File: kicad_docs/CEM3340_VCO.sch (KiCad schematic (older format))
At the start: 94 parts, among them J1 tuning controls, J2 1 v/oct inputs, J3 linear FM input, J4 sync input, J5 PWM inputs, J6 power input, Q1 MMDT3904, U1 L78L10_SOT89, U2 MC7905, U3 REF02AU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

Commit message: extract circuit blocks into separate schem pages
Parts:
- removed C1, C16, C17: 100nF, Capacitor_SMD:C_0805_2012Metric_Pad1.15x1.40mm_HandSolder, symbol Device:C
- removed C10, C13, C14: 1nF, Capacitor_SMD:C_0805_2012Metric_Pad1.15x1.40mm_HandSolder, symbol Device:C
- removed C11, C15: 10nF, Capacitor_SMD:C_0805_2012Metric_Pad1.15x1.40mm_HandSolder, symbol Device:C
- removed C20: 560pF, Capacitor_SMD:C_0805_2012Metric_Pad1.15x1.40mm_HandSolder, symbol Device:C
- removed C25: 10pF, Capacitor_SMD:C_0805_2012Metric_Pad1.15x1.40mm_HandSolder, symbol Device:C
- removed J1: tuning controls, Connector_PinHeader_2.54mm:PinHeader_1x05_P2.54mm_Vertical, symbol Connector_Generic:Conn_01x05
- removed J2: 1 v/oct inputs, Connector_PinHeader_2.54mm:PinHeader_1x04_P2.54mm_Vertical, symbol Connector_Generic:Conn_01x04
- removed J3: linear FM input, Connector_PinHeader_2.54mm:PinHeader_1x02_P2.54mm_Vertical, symbol Connector_Generic:Conn_01x02
- removed J4: sync input, Connector_PinHeader_2.54mm:PinHeader_1x02_P2.54mm_Vertical, symbol Connector_Generic:Conn_01x02
- removed J5: PWM inputs, Connector_PinHeader_2.54mm:PinHeader_1x05_P2.54mm_Vertical, symbol Connector_Generic:Conn_01x05
- removed JP1: sync sel 1, Jumper:SolderJumper-3_P1.3mm_Open_RoundedPad1.0x1.5mm, symbol Jumper:SolderJumper_3_Open
- removed JP2: sync sel 2, Jumper:SolderJumper-3_P1.3mm_Open_RoundedPad1.0x1.5mm, symbol Jumper:SolderJumper_3_Open
- removed Q1: MMDT3904, Package_TO_SOT_SMD:SOT-363_SC-70-6_Handsoldering, symbol Transistor_BJT:MMDT3904
- removed R1, R2, R29, R3, R31, R33, R37, R38, R7: 100k, Resistor_SMD:R_0805_2012Metric_Pad1.15x1.40mm_HandSolder, symbol Device:R
- removed R10, R9: 5k6, Resistor_SMD:R_0805_2012Metric_Pad1.15x1.40mm_HandSolder, symbol Device:R
- removed R11, R8: 1M, Resistor_SMD:R_0805_2012Metric_Pad1.15x1.40mm_HandSolder, symbol Device:R
- removed R12, R13: 51k, Resistor_SMD:R_0805_2012Metric_Pad1.15x1.40mm_HandSolder, symbol Device:R
- removed R15, R26: 18k, Resistor_SMD:R_0805_2012Metric_Pad1.15x1.40mm_HandSolder, symbol Device:R
- removed R16: 82k, Resistor_SMD:R_0805_2012Metric_Pad1.15x1.40mm_HandSolder, symbol Device:R
- removed R17, R20: 470, Resistor_SMD:R_0805_2012Metric_Pad1.15x1.40mm_HandSolder, symbol Device:R
- removed R19: 680k, Resistor_SMD:R_0805_2012Metric_Pad1.15x1.40mm_HandSolder, symbol Device:R
- removed R21: 1k62, Resistor_SMD:R_0805_2012Metric_Pad1.15x1.40mm_HandSolder, symbol Device:R
- removed R22: 27k, Resistor_SMD:R_0805_2012Metric_Pad1.15x1.40mm_HandSolder, symbol Device:R
- removed R23, R28: 2k2, Resistor_SMD:R_0805_2012Metric_Pad1.15x1.40mm_HandSolder, symbol Device:R
- removed R24, R27, R34: 10k, Resistor_SMD:R_0805_2012Metric_Pad1.15x1.40mm_HandSolder, symbol Device:R
- removed R25: 390, Resistor_SMD:R_0805_2012Metric_Pad1.15x1.40mm_HandSolder, symbol Device:R
- removed R30, R32, R4, R5: ???, Resistor_SMD:R_0805_2012Metric_Pad1.15x1.40mm_HandSolder, symbol Device:R
- removed R35, R36: 11k, Resistor_SMD:R_0805_2012Metric_Pad1.15x1.40mm_HandSolder, symbol Device:R
- removed R39: 10M, Resistor_SMD:R_0805_2012Metric_Pad1.15x1.40mm_HandSolder, symbol Device:R
- removed R40, R44: R, Resistor_SMD:R_0805_2012Metric_Pad1.15x1.40mm_HandSolder, symbol Device:R
- removed R41, R42, R43: 1k, Resistor_SMD:R_0805_2012Metric_Pad1.15x1.40mm_HandSolder, symbol Device:R
- removed R6: 270k, Resistor_SMD:R_0805_2012Metric_Pad1.15x1.40mm_HandSolder, symbol Device:R
- removed RV1: 20k, Potentiometer_THT:Potentiometer_Bourns_3296W_Vertical, symbol Device:R_POT_TRIM
- removed RV2: 5k, Potentiometer_THT:Potentiometer_Bourns_3296W_Vertical, symbol Device:R_POT_TRIM
- removed RV3, RV5, RV6: 50k, Potentiometer_THT:Potentiometer_Bourns_3296W_Vertical, symbol Device:R_POT_TRIM
- removed RV4: 500, Potentiometer_THT:Potentiometer_Bourns_3296W_Vertical, symbol Device:R_POT_TRIM
- removed TP1, TP2: TestPoint, TestPoint:TestPoint_Keystone_5000-5004_Miniature, symbol Connector:TestPoint
- removed U4: CEM3340, Package_DIP:DIP-16_W7.62mm, symbol my_parts:CEM3340
- removed unit 1 of U5
- removed unit 2 of U5
- removed unit 2 of U6
- removed unit 1 of U6
- removed unit 1 of U7
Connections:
- net buffered_pulse_out renamed Waveshapers/10vpp_pulse_v_out
- net buffered_saw_out renamed Waveshapers/10vpp_saw_v_out
- net buffered_sine_out renamed Waveshapers/10vpp_sine_v_out
- net buffered_tri_out renamed Waveshapers/10vpp_triangle_v_out
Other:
- note removed: "PWM CV"
- note removed: "Power supply"
- note removed: "Signal Inputs"
- note removed: "Signal Outputs"
- note removed: "VCO Core"
- note removed: "Waveshapers/Output Buffers"
- note removed: "about ???vpp"
- note removed: "coarse tune"
- note removed: "fine tune"
- note removed: "freq offset adj"
- note removed: "high freq adj"
- note removed: "manual pulse width"
- note removed: "pulse shaper/buffer"
- note removed: "saw wave amp/buffer"
- note removed: "scale adj"
- note removed: "sine shape adj"
- note removed: "sine symm adj"
- note removed: "tempco adj"
- note removed: "timing cap"
- note removed: "tri to sine shaper"
- note removed: "triangle wave amp/buffer"
- moved on the sheet: C12, C18, C19, C2, C21, C22, C23, C24, C3, C4, C5, C6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

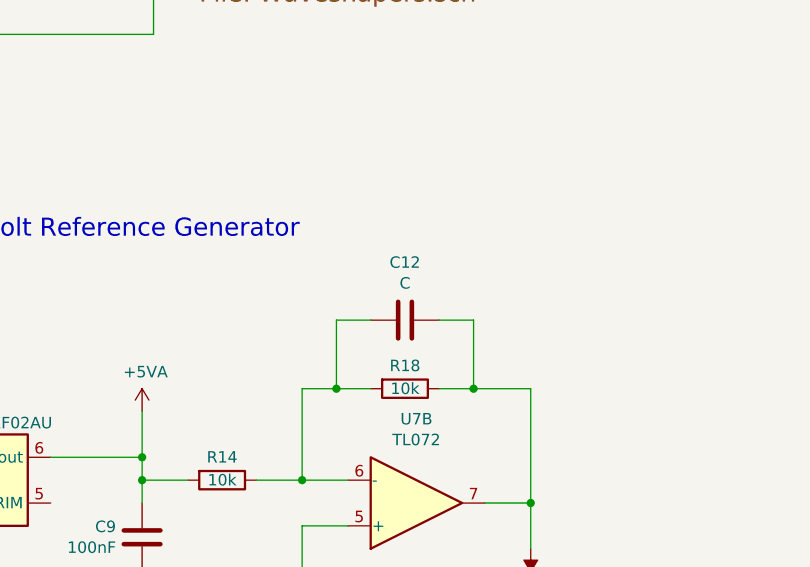
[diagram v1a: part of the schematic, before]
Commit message: update and fill in some resistor values
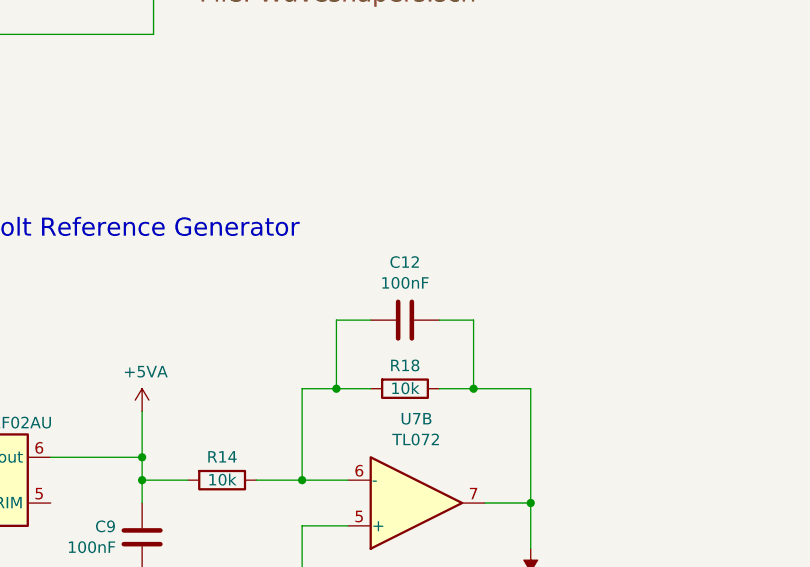
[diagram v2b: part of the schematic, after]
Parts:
- C12: value C -> 100nF
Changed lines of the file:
@@
 P 7900 4000
 F 0 "C12" V 7648 4000 50  0000 C CNN
-F 1 "C" V 7739 4000 50  0000 C CNN
+F 1 "100nF" V 7739 4000 50  0000 C CNN
 F 2 "Capacitor_SMD:C_0805_2012Metric_Pad1.15x1.40mm_HandSolder" H 7938 3850 50  0001 C CNN
 F 3 "~" H 7900 4000 50  0001 C CNN

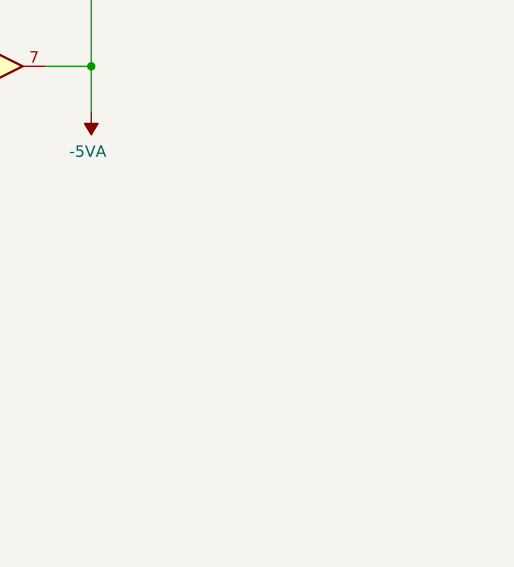
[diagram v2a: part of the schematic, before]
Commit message: finalize some values, update documentation
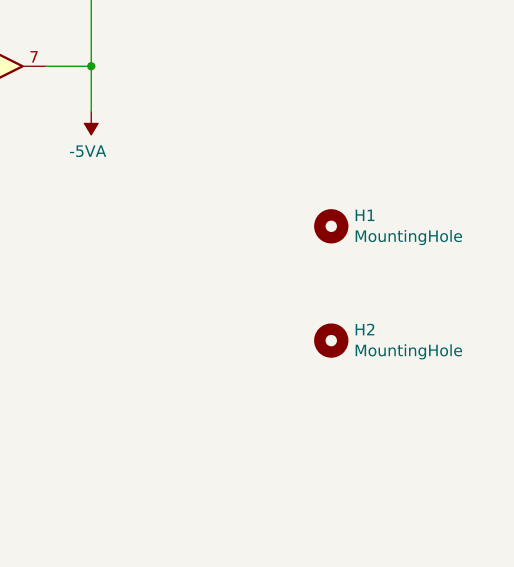
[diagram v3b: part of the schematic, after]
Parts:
- added H1, H2: MountingHole, MountingHole:MountingHole_3.2mm_M3, symbol Mechanical:MountingHole
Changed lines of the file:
@@
 Wire Wire Line
 	8500 1450 9000 1450
+$Comp
+L Mechanical:MountingHole H1
+U 1 1 5EF791CF
+P 9500 5500
+F 0 "H1" H 9600 5546 50  0000 L CNN
+F 1 "MountingHole" H 9600 5455 50  0000 L CNN
+F 2 "MountingHole:MountingHole_3.2mm_M3" H 9500 5500 50  0001 C CNN
+F 3 "~" H 9500 5500 50  0001 C CNN
+	1    9500 5500
+	1    0    0    -1
+$EndComp
+$Comp
+L Mechanical:MountingHole H2
+U 1 1 5EF79872
+P 9500 6000
+F 0 "H2" H 9600 6046 50  0000 L CNN
+F 1 "MountingHole" H 9600 5955 50  0000 L CNN
+F 2 "MountingHole:MountingHole_3.2mm_M3" H 9500 6000 50  0001 C CNN
+F 3 "~" H 9500 6000 50  0001 C CNN
+	1    9500 6000
+	1    0    0    -1
+$EndComp
 $EndSCHEMATC
